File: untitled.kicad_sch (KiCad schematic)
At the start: 47 parts, among them Q1 NMOS, Q2 NMOS, Q3 NMOS, Q4 NMOS, U17 OPA388, U3 MAX9939, U4 TLV3501AID, U5 DGS0010A, U6 OPA2392, U7 ADC10065

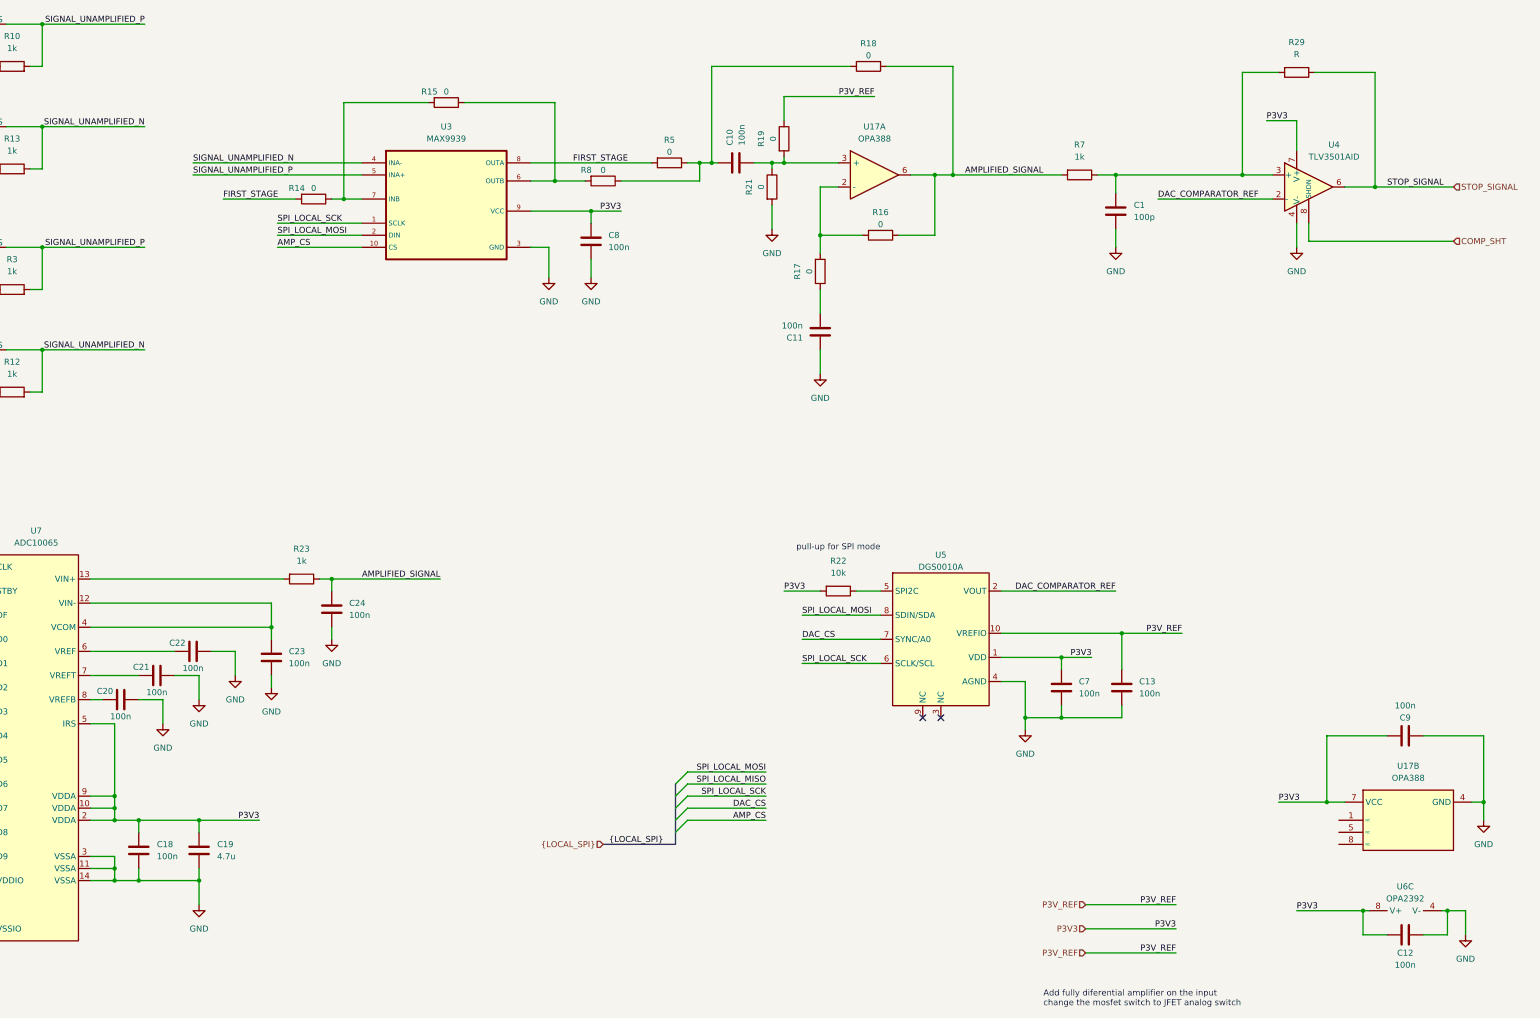
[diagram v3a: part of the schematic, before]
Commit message: schematic ready, basic layout done
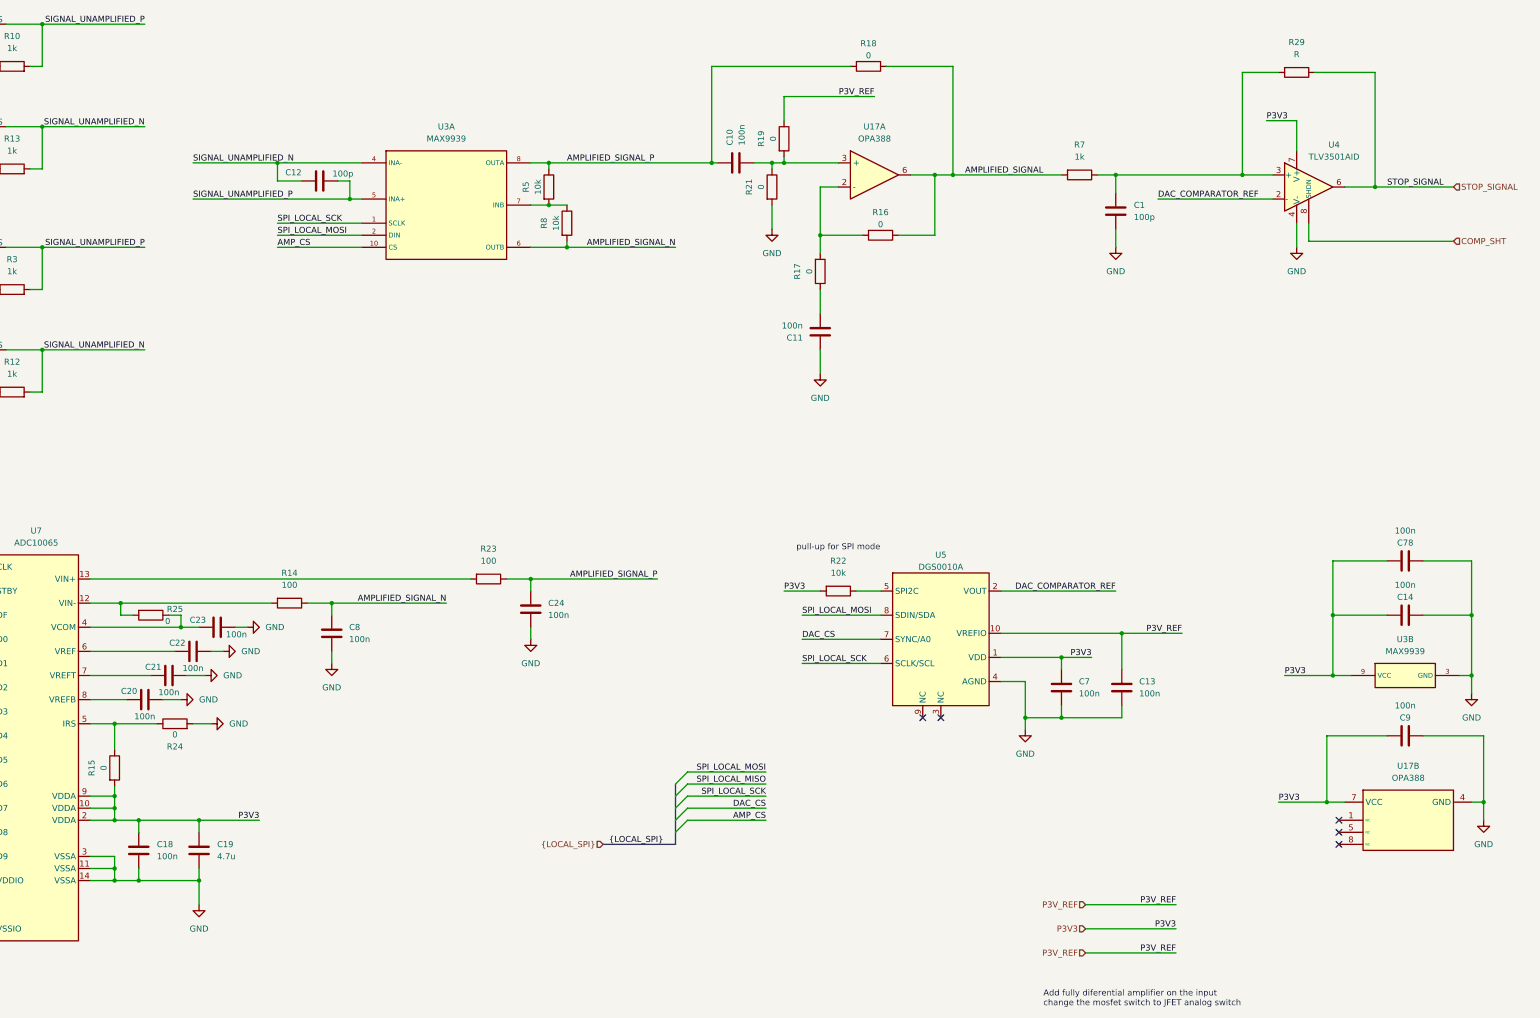
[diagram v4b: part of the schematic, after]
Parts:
- removed U6: OPA2392, Package_SO:SOIC-8_3.9x4.9mm_P1.27mm, symbol Device:Opamp_Dual
- added C14, C78: 100n, Capacitor_SMD:C_0603_1608Metric_Pad1.08x0.95mm_HandSolder, symbol Device:C
- added R24, R25: 0, Resistor_SMD:R_0603_1608Metric_Pad0.98x0.95mm_HandSolder, symbol Device:R
- added unit 2 of U3
- C12: value 100n -> 100p
- R14: value 0 -> 100; now left out of the parts list
- R23: value 1k -> 100
- R5, R8: value 0 -> 10k
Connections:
- net AMPLIFIED_SIGNAL: no longer C24.2, R23.1
- net GND: now also C14.2, C78.2, R24.2, U3.3 (GND); no longer C12.2, U3.3 (GND)
- net P3V3: now also R15.2, C14.1, C78.1, U3.9 (VCC); no longer C12.1, C8.2, U3.9 (VCC), U7.5 (IRS)
- net SIGNAL_UNAMPLIFIED_N: now also C12.2
- net SIGNAL_UNAMPLIFIED_P: now also C12.1
- net AMPLIFIED_SIGNAL_N: now reaches R8.2, U3.6 (OUTB)
- net AMPLIFIED_SIGNAL_N: now also C8.2, R14.1; no longer R15.1
- net at C23.2, U7.4 (VCOM): now also R25.1; no longer U7.12 (VIN-)
- net AMPLIFIED_SIGNAL_P: now reaches C10.2, R18.2, R5.1
- net AMPLIFIED_SIGNAL_P: now also C24.2, R23.1, U3.8 (OUTA); no longer R8.1
- removed net FIRST_STAGE: R14.2, R5.2, U3.8 (OUTA)
- new net: R5.2, R8.1, U3.7 (INB)
- new net: R15.1, R24.1, U7.5 (IRS)
- new net: R14.2, R25.2, U7.12 (VIN-)
- no-connect marks 2 -> 5
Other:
- moved on the sheet: C20, C21, C23, C24, R23

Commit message: before changing MUX
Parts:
- added R72: 0, Resistor_SMD:R_0603_1608Metric_Pad0.98x0.95mm_HandSolder, symbol Device:R
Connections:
- net AMPLIFIED_SIGNAL: now also R72.1; no longer R16.1, U17.6
- net GND: now also R10.2, R12.2, R13.2, R3.2
- net SIGNAL_UNAMPLIFIED_N: no longer R12.2, R13.2
- net SIGNAL_UNAMPLIFIED_P: no longer R10.2, R3.2
- new net: R16.1, R72.2, U17.6

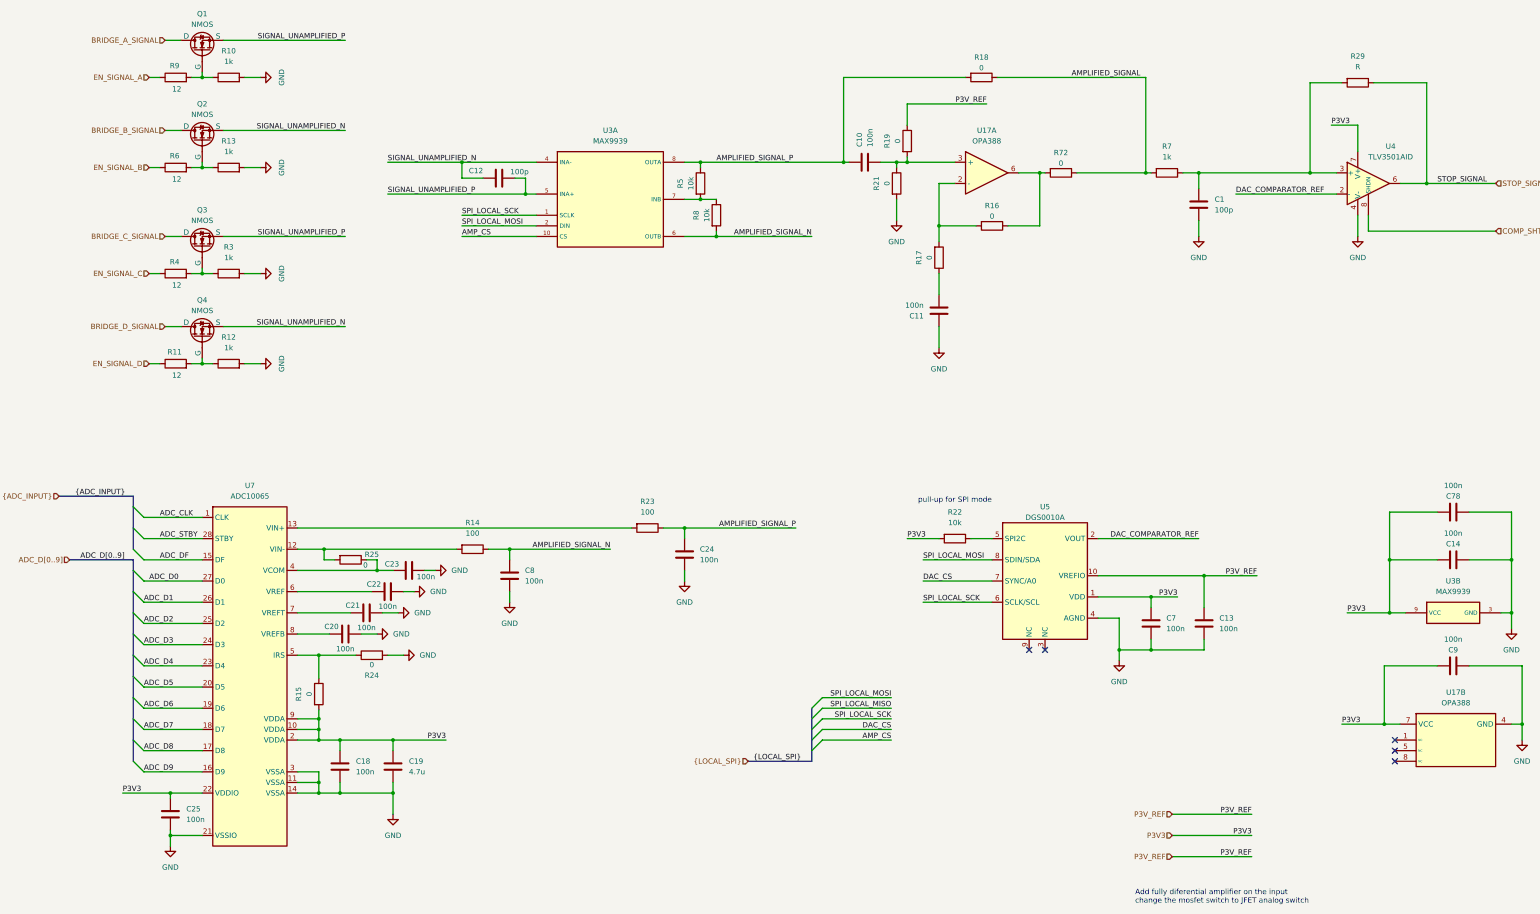
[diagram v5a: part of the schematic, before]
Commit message: no errors schematic, basic routing done
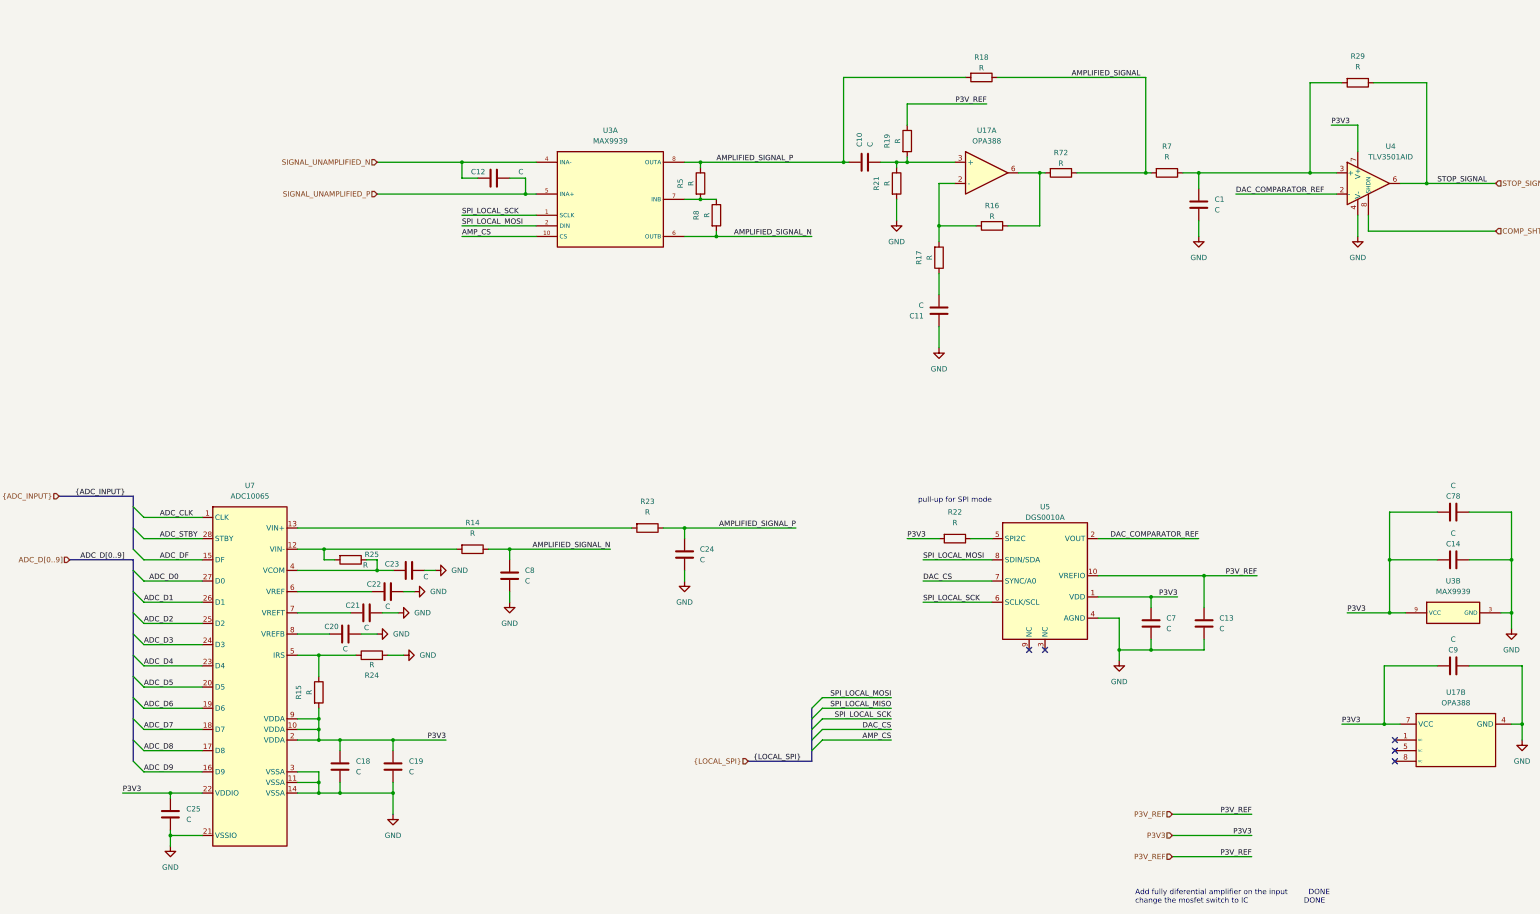
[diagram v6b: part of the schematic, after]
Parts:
- removed Q1, Q2, Q3, Q4: NMOS, Package_TO_SOT_SMD:SOT-23_Handsoldering, symbol Simulation_SPICE:NMOS
- removed R10, R12, R13, R3: 1k, Resistor_SMD:R_0603_1608Metric_Pad0.98x0.95mm_HandSolder, symbol Device:R
- removed R11, R4, R6, R9: 12, Resistor_SMD:R_0603_1608Metric_Pad0.98x0.95mm_HandSolder, symbol Device:R
- C1, C12: value 100p -> C
- C10, C11, C13, C14, C18, C20, C21, C22, C23, C24, C25, C7, C78, C8, C9: value 100n -> C
- C19: value 4.7u -> C
- R14, R23: value 100 -> R
- R15, R16, R17, R18, R19, R21, R24, R25, R72: value 0 -> R
- R22, R5, R8: value 10k -> R
- R7: value 1k -> R
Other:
- note added: "Add fully diferential amplifier on the input DONE change the mosfet switch to IC DONE"
- note removed: "Add fully diferential amplifier on the input change the mosfet switch to JFET analog switch"
- moved on the sheet: C12

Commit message: DONE - before checking
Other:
- note added: "ADC"
- note added: "Amplification and comparator"
- note added: "DAC"
- note added: "Power pins and hierarchy"
- moved on the sheet: C1, C10, C11, C12, C13, C14, C18, C19, C20, C21, C22, C23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
